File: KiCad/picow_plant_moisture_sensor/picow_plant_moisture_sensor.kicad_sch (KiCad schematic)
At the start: 28 parts, among them J1 Conn_01x03, J10 Conn_01x03, J11 Conn_01x03, J12 Conn_01x03, J13 Conn_01x03, J14 ADS1115, J15 ADS1115, J16 ADS1115, J2 Conn_01x03, J3 Conn_01x03, J4 Conn_01x03, J5 Conn_01x03, J6 Conn_01x03, J7 Conn_02x03_Odd_Even, J8 Conn_01x03, J9 Conn_01x03, SW1 SW_Push, SW2 SW_Push, SW3 SW_Push, SW4 SW_Push, U2 PicoW

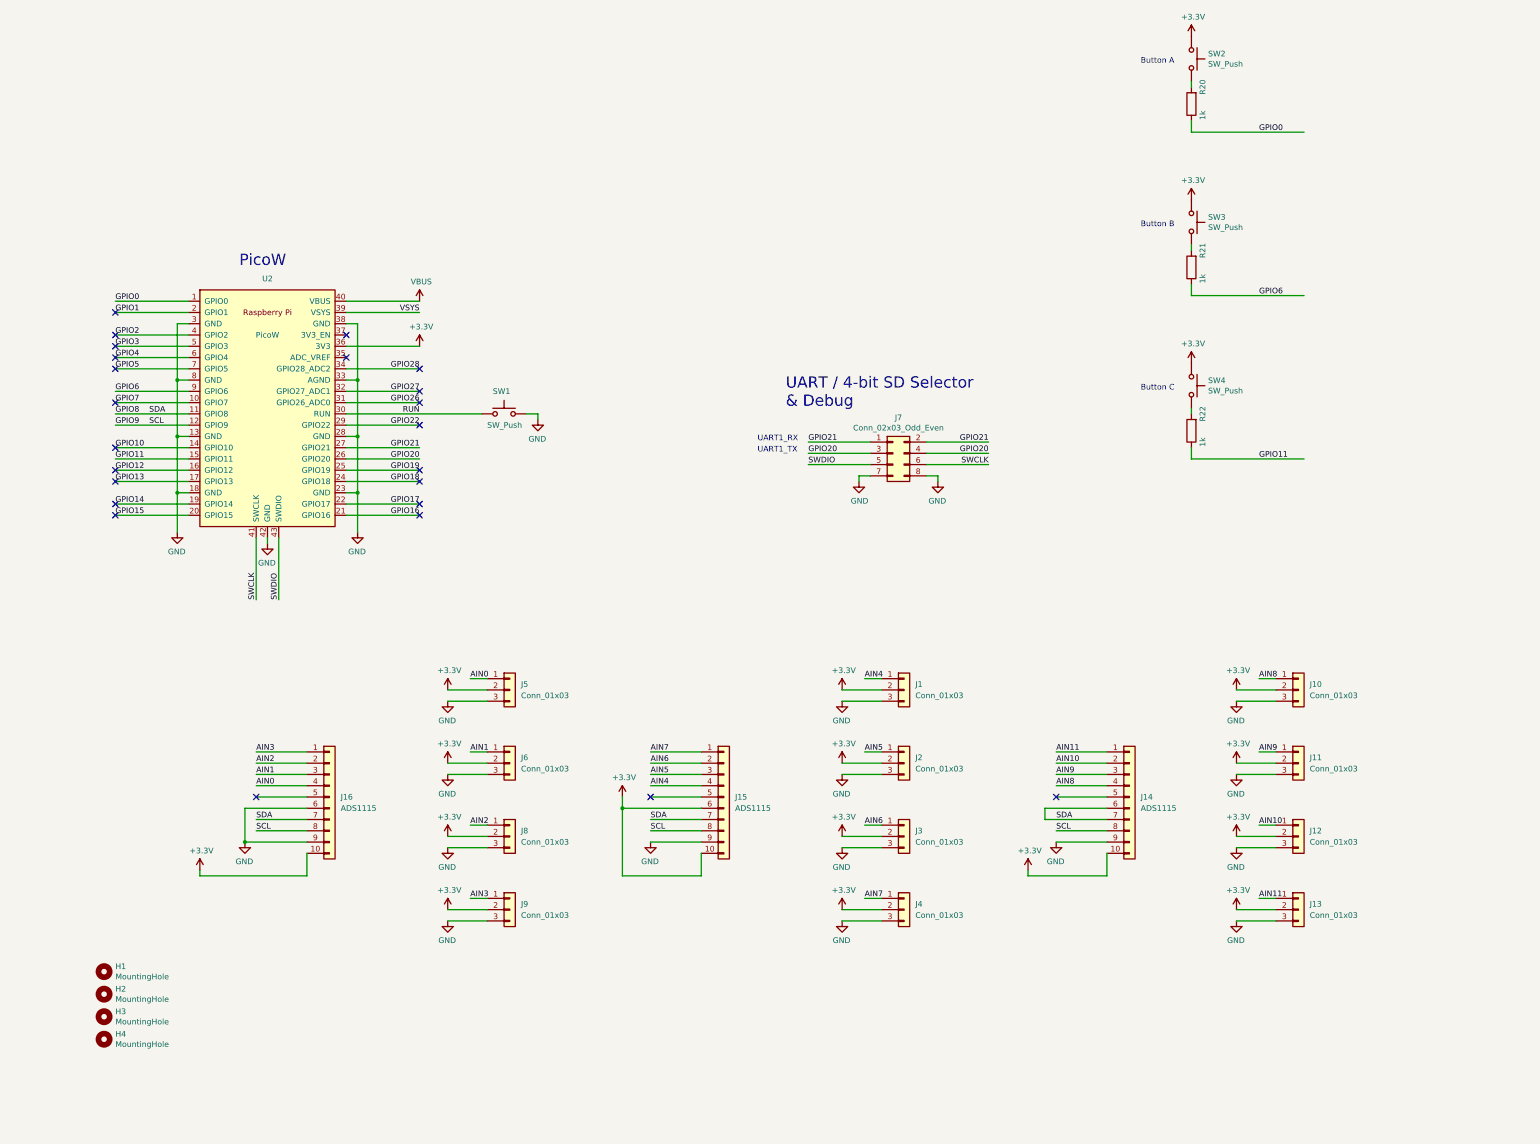
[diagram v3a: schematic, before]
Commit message: No traces
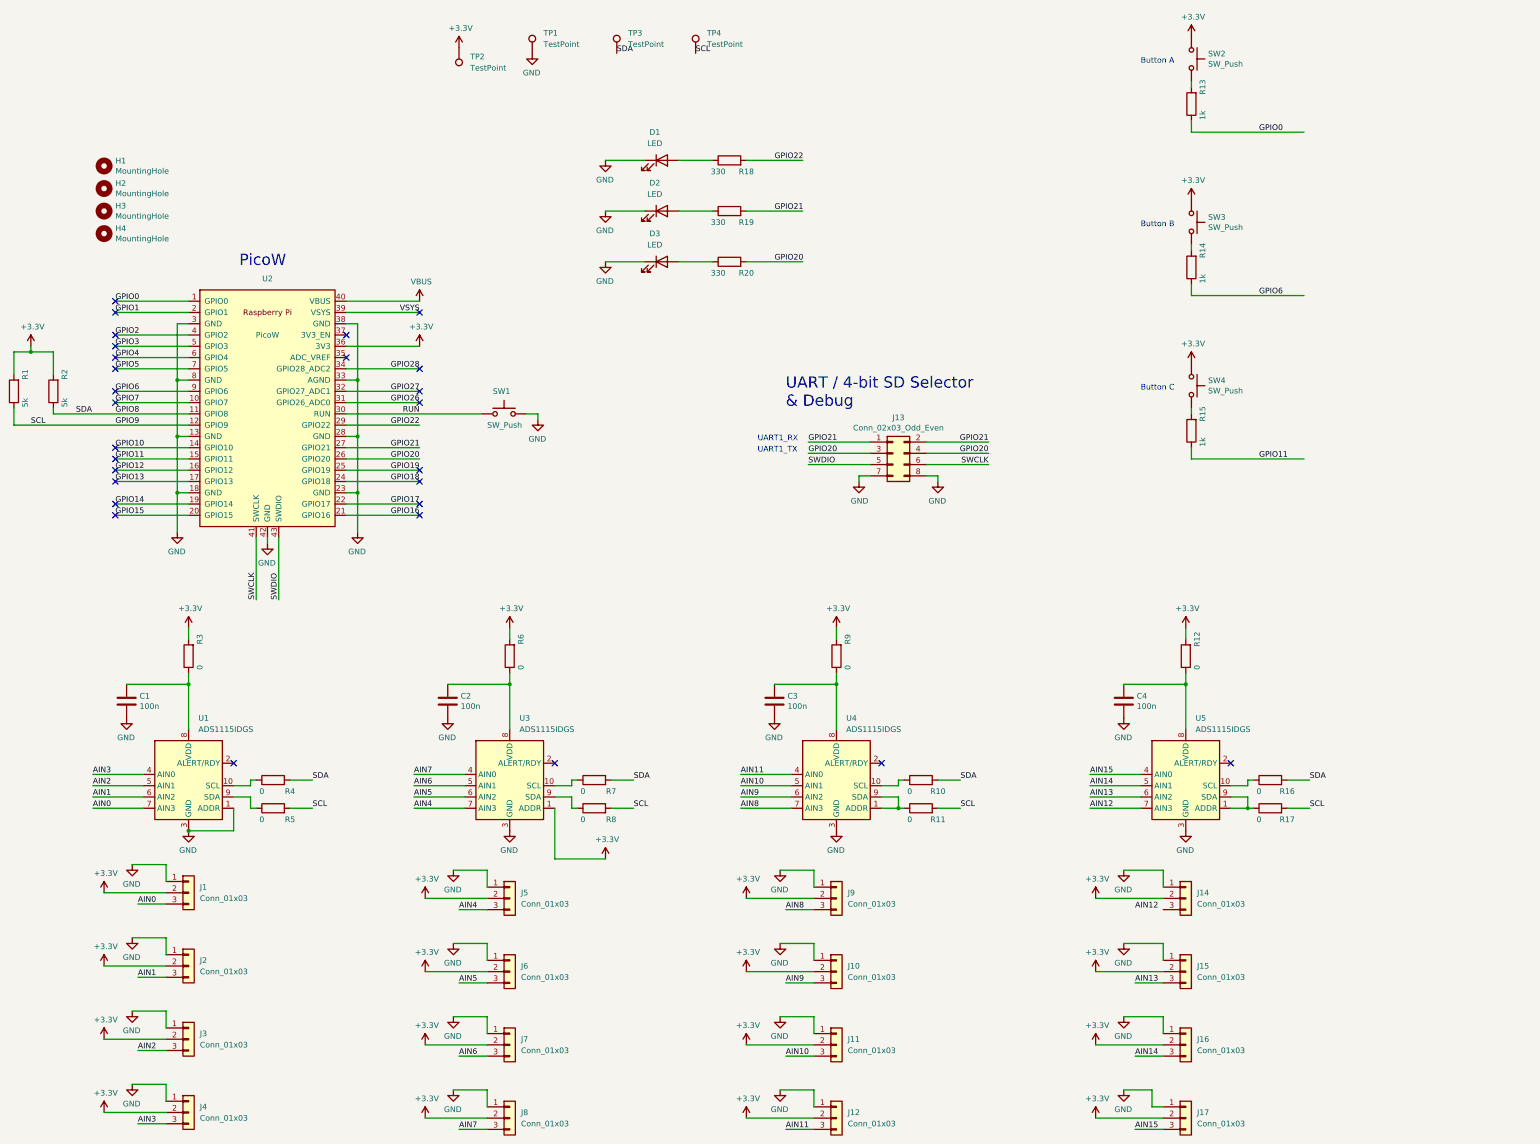
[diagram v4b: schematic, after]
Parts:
- removed J14, J15, J16: ADS1115, Connector_PinHeader_2.54mm:PinHeader_1x10_P2.54mm_Vertical, symbol Connector_Generic:Conn_01x10
- added C1, C2, C3, C4: 100n, Capacitor_SMD:C_0402_1005Metric, symbol Device:C
- added D1, D2, D3: LED, LED_SMD:LED_0402_1005Metric, symbol Device:LED
- added J14, J15, J16, J17: Conn_01x03, Connector_JST:JST_PH_B3B-PH-K_1x03_P2.00mm_Vertical, symbol Connector_Generic:Conn_01x03
- added R1, R2: 5k, Resistor_SMD:R_0402_1005Metric, symbol Device:R
- added R10, R11, R12, R16, R17, R3, R4, R5, R6, R7, R8, R9: 0, Resistor_SMD:R_0603_1608Metric, symbol Device:R
- added R18, R19, R20: 330, Resistor_SMD:R_0402_1005Metric, symbol Device:R
- added TP1, TP2, TP3, TP4: TestPoint, TestPoint:TestPoint_Pad_D2.0mm, symbol Connector:TestPoint
- added U1, U3, U4, U5: ADS1115IDGS, Package_SO:TSSOP-10_3x3mm_P0.5mm, symbol Analog_ADC:ADS1115IDGS
- J1: renamed from J5; footprint Connector_PinHeader_2.54mm:PinHeader_1x03_P2.54mm_Vertical -> Connector_JST:JST_PH_B3B-PH-K_1x03_P2.00mm_Vertical
- J10: renamed from J11; footprint Connector_PinHeader_2.54mm:PinHeader_1x03_P2.54mm_Vertical -> Connector_JST:JST_PH_B3B-PH-K_1x03_P2.00mm_Vertical
- J11: renamed from J12; footprint Connector_PinHeader_2.54mm:PinHeader_1x03_P2.54mm_Vertical -> Connector_JST:JST_PH_B3B-PH-K_1x03_P2.00mm_Vertical
- J12: renamed from J13; footprint Connector_PinHeader_2.54mm:PinHeader_1x03_P2.54mm_Vertical -> Connector_JST:JST_PH_B3B-PH-K_1x03_P2.00mm_Vertical
- J2: renamed from J6; footprint Connector_PinHeader_2.54mm:PinHeader_1x03_P2.54mm_Vertical -> Connector_JST:JST_PH_B3B-PH-K_1x03_P2.00mm_Vertical
- J3: renamed from J8; footprint Connector_PinHeader_2.54mm:PinHeader_1x03_P2.54mm_Vertical -> Connector_JST:JST_PH_B3B-PH-K_1x03_P2.00mm_Vertical
- J4: renamed from J9; footprint Connector_PinHeader_2.54mm:PinHeader_1x03_P2.54mm_Vertical -> Connector_JST:JST_PH_B3B-PH-K_1x03_P2.00mm_Vertical
- J5: renamed from J1; footprint Connector_PinHeader_2.54mm:PinHeader_1x03_P2.54mm_Vertical -> Connector_JST:JST_PH_B3B-PH-K_1x03_P2.00mm_Vertical
- J6: renamed from J2; footprint Connector_PinHeader_2.54mm:PinHeader_1x03_P2.54mm_Vertical -> Connector_JST:JST_PH_B3B-PH-K_1x03_P2.00mm_Vertical
- J7: renamed from J3; footprint Connector_PinHeader_2.54mm:PinHeader_1x03_P2.54mm_Vertical -> Connector_JST:JST_PH_B3B-PH-K_1x03_P2.00mm_Vertical
- J8: renamed from J4; footprint Connector_PinHeader_2.54mm:PinHeader_1x03_P2.54mm_Vertical -> Connector_JST:JST_PH_B3B-PH-K_1x03_P2.00mm_Vertical
- J9: renamed from J10; footprint Connector_PinHeader_2.54mm:PinHeader_1x03_P2.54mm_Vertical -> Connector_JST:JST_PH_B3B-PH-K_1x03_P2.00mm_Vertical
- renumbered J7 to J13, R20 to R13, R21 to R14, R22 to R15
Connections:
- net +3V3: now also J14.2 (Pin_2), J15.2 (Pin_2), J16.2 (Pin_2), J17.2 (Pin_2), R1.2, R12.2, R2.2, R3.2, R6.2, R9.2, TP2.1, U3.1 (ADDR)
- net AIN0: now also J1.3 (Pin_3), U1.7 (AIN3); no longer J1.1 (Pin_1)
- net AIN1: now also J2.3 (Pin_3), U1.6 (AIN2); no longer J2.1 (Pin_1)
- net AIN10: now also J11.3 (Pin_3), U4.5 (AIN1); no longer J11.1 (Pin_1)
- net AIN11: now also J12.3 (Pin_3), U4.4 (AIN0); no longer J12.1 (Pin_1)
- net AIN2: now also J3.3 (Pin_3), U1.5 (AIN1); no longer J3.1 (Pin_1)
- net AIN3: now also J4.3 (Pin_3), U1.4 (AIN0); no longer J4.1 (Pin_1)
- net AIN4: now also J5.3 (Pin_3), U3.7 (AIN3); no longer J5.1 (Pin_1)
- net AIN5: now also J6.3 (Pin_3), U3.6 (AIN2); no longer J6.1 (Pin_1)
- net AIN6: now also J7.3 (Pin_3), U3.5 (AIN1); no longer J7.1 (Pin_1)
- net AIN7: now also J8.3 (Pin_3), U3.4 (AIN0); no longer J8.1 (Pin_1)
- net AIN8: now also J9.3 (Pin_3), U4.7 (AIN3); no longer J9.1 (Pin_1)
- net AIN9: now also J10.3 (Pin_3), U4.6 (AIN2); no longer J10.1 (Pin_1)
- net GND: now also J1.1 (Pin_1), J10.1 (Pin_1), J11.1 (Pin_1), J12.1 (Pin_1), J2.1 (Pin_1), J3.1 (Pin_1), J4.1 (Pin_1), J5.1 (Pin_1), J6.1 (Pin_1), J7.1 (Pin_1), J8.1 (Pin_1), J9.1 (Pin_1), C1.2, C2.2, C3.2, C4.2, D1.1 (K), D2.1 (K), D3.1 (K), J14.1 (Pin_1), J15.1 (Pin_1), J16.1 (Pin_1), J17.1 (Pin_1), TP1.1, U1.1 (ADDR), U1.3 (GND), U3.3 (GND), U4.3 (GND), U5.3 (GND); no longer J1.3 (Pin_3), J10.3 (Pin_3), J11.3 (Pin_3), J12.3 (Pin_3), J2.3 (Pin_3), J3.3 (Pin_3), J4.3 (Pin_3), J5.3 (Pin_3), J6.3 (Pin_3), J7.3 (Pin_3), J8.3 (Pin_3), J9.3 (Pin_3)
- net GPIO20: now also R20.2
- net GPIO21: now also R19.2
- net GPIO22: now also R18.2
- net GPIO8: now also R10.2, R16.2, R2.1, R4.2, R7.2, TP3.1
- net GPIO9: now also R1.1, R11.2, R17.2, R5.2, R8.2, TP4.1
- new net: C1.1, R3.1, U1.8 (VDD)
- new net: R10.1, U4.10 (SCL)
- new net: C4.1, R12.1, U5.8 (VDD)
- new net: C2.1, R6.1, U3.8 (VDD)
- new net: R4.1, U1.10 (SCL)
- new net: R5.1, U1.9 (SDA)
- new net: R16.1, U5.10 (SCL)
- new net: R17.1, U5.1 (ADDR), U5.9 (SDA)
- new net: D3.2 (A), R20.1
- new net: D2.2 (A), R19.1
- new net: R7.1, U3.10 (SCL)
- new net: R8.1, U3.9 (SDA)
- new net: C3.1, R9.1, U4.8 (VDD)
- new net: R11.1, U4.1 (ADDR), U4.9 (SDA)
- new net: D1.2 (A), R18.1
- new net AIN12: U5.7 (AIN3)
- new net AIN13: J15.3 (Pin_3), U5.6 (AIN2)
- new net AIN14: J16.3 (Pin_3), U5.5 (AIN1)
- new net AIN15: J17.3 (Pin_3), U5.4 (AIN0)
- no-connect marks 24 -> 28
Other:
- company: Raspberry Pi Ltd -> Andreas Andersson
- title: RPI-PWVSA    VGA, SD Card & Audio Demo Board for Pico W -> Analog Sensor Board for Pico W
- moved on the sheet: H1, H2, H3, H4, J1, J10, J11, J12, J2, J3, J4, J5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

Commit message: Routing done
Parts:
- removed TP3, TP4: TestPoint, TestPoint:TestPoint_Pad_D2.0mm, symbol Connector:TestPoint
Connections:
- net AIN12: now also J14.3 (Pin_3)
- net GPIO2: now also R18.2
- net GPIO20: no longer R20.2
- net GPIO21: no longer R19.2
- net GPIO22: no longer R18.2
- net GPIO3: now also R19.2
- net GPIO4: now also R20.2
- no-connect marks 28 -> 25
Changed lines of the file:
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@@
   (junction (at 53.34 107.95) (diameter 0) (color 0 0 0 0)
   )
+  (no_connect (at 107.95 105.41))
   (no_connect (at 39.37 105.41))
   (no_connect (at 212.09 194.31))
@@
   (no_connect (at 39.37 125.73))
   (no_connect (at 91.44 102.87))
-  (no_connect (at 107.95 113.03))
   (no_connect (at 107.95 128.27))
   (no_connect (at 39.37 110.49))
-  (no_connect (at 39.37 97.79))
   (no_connect (at 290.83 194.31))
+  (no_connect (at 107.95 113.03))
   (no_connect (at 107.95 135.89))
   (no_connect (at 39.37 128.27))
@@
   (no_connect (at 39.37 113.03))
   (no_connect (at 138.43 194.31))
-  (no_connect (at 39.37 102.87))
   (no_connect (at 39.37 130.81))
   (no_connect (at 39.37 123.19))
@@
   (no_connect (at 107.95 110.49))
   (no_connect (at 39.37 135.89))
-  (no_connect (at 107.95 105.41))
   (no_connect (at 39.37 138.43))
-  (no_connect (at 39.37 100.33))
   (no_connect (at 107.95 138.43))
   (wire (pts (xy 132.08 115.57) (xy 134.62 115.57))
@@
     (stroke (width 0) (type default))
   )
+  (wire (pts (xy 269.24 227.33) (xy 275.59 227.33))
+    (stroke (width 0) (type default))
+  )
   (wire (pts (xy 50.8 250.19) (xy 43.18 250.19))
     (stroke (width 0) (type default))
@@
     (effects (font (size 1.27 1.27)) (justify right bottom))
   )
-  (label "SCL" (at 170.18 34.29 0) (fields_autoplaced)
-    (effects (font (size 1.27 1.27)) (justify left bottom))
-  )
-  (label "GPIO20" (at 187.96 81.28 0) (fields_autoplaced)
+  (label "GPIO4" (at 187.96 81.28 0) (fields_autoplaced)
     (effects (font (size 1.27 1.27)) (justify left bottom))
   )
@@
     (effects (font (size 1.27 1.27)) (justify right bottom))
   )
-  (label "GPIO21" (at 187.96 69.85 0) (fields_autoplaced)
+  (label "GPIO3" (at 187.96 69.85 0) (fields_autoplaced)
     (effects (font (size 1.27 1.27)) (justify left bottom))
   )
@@
     (effects (font (size 1.27 1.27)) (justify left bottom))
   )
-  (label "SDA" (at 152.4 34.29 0) (fields_autoplaced)
-    (effects (font (size 1.27 1.27)) (justify left bottom))
-  )
   (label "SCL" (at 20.32 118.11 0) (fields_autoplaced)
     (effects (font (size 1.27 1.27)) (justify left bottom))
   )
-  (label "GPIO22" (at 187.96 58.42 0) (fields_autoplaced)
+  (label "GPIO2" (at 187.96 58.42 0) (fields_autoplaced)
     (effects (font (size 1.27 1.27)) (justify left bottom))
   )
@@
     )
   )
-  (symbol (lib_id "Connector:TestPoint") (at 152.4 34.29 0) (unit 1)
-    (in_bom yes) (on_board yes) (dnp no) (fields_autoplaced)
-    (property "Reference" "TP3" (at 154.94 29.718 0)
-      (effects (font (size 1.27 1.27)) (justify left))
-    )
-    (property "Value" "TestPoint" (at 154.94 32.258 0)
-      (effects (font (size 1.27 1.27)) (justify left))
-    )
-    (property "Footprint" "TestPoint:TestPoint_Pad_D2.0mm" (at 157.48 34.29 0)
-      (effects (font (size 1.27 1.27)) hide)
-    )
-    (property "Datasheet" "~" (at 157.48 34.29 0)
-      (effects (font (size 1.27 1.27)) hide)
-    )
-    (pin "1")
-    (instances
-      (project "picow_plant_moisture_sensor"
-        (path "/7e7c068a-a341-4358-ab45-53bb7a793d6f"
-          (reference "TP3") (unit 1)
-        )
-      )
-    )
-  )
   (symbol (lib_id "power:+3.3V") (at 36.83 240.03 0) (unit 1)
     (in_bom yes) (on_board yes) (dnp no)
@@
         )
       )
-    )
-  )
-  (symbol (lib_id "Connector:TestPoint") (at 170.18 34.29 0) (unit 1)
-    (in_bom yes) (on_board yes) (dnp no) (fields_autoplaced)
-    (property "Reference" "TP4" (at 172.72 29.718 0)
-      (effects (font (size 1.27 1.27)) (justify left))
-    )
-    (property "Value" "TestPoint" (at 172.72 32.258 0)
-      (effects (font (size 1.27 1.27)) (justify left))
-    )
-    (property "Footprint" "TestPoint:TestPoint_Pad_D2.0mm" (at 175.26 34.29 0)
-      (effects (font (size 1.27 1.27)) hide)
-    )
-    (property "Datasheet" "~" (at 175.26 34.29 0)
-      (effects (font (size 1.27 1.27)) hide)
-    )
-    (pin "1")
-    (instances
-      (project "picow_plant_moisture_sensor"
-        (path "/7e7c068a-a341-4358-ab45-53bb7a793d6f"
-          (reference "TP4") (unit 1)
-        )
-      )
